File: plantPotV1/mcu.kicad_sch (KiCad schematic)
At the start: 1 part, among them U3 NUCLEO-L4R5ZI-P

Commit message: changed to meet proposal
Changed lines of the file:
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@@
 		(comment 4 "Stanford University")
+	)
+	(hierarchical_label "CS"
+		(shape output)
+		(at 134.62 52.07 0)
+		(fields_autoplaced yes)
+		(effects
+			(font
+				(size 1.27 1.27)
+			)
+			(justify left)
+		)
 	)
 	(hierarchical_label "SDA"
 		(shape output)
 		(at 110.49 50.8 0)
+		(fields_autoplaced yes)
+		(effects
+			(font
+				(size 1.27 1.27)
+			)
+			(justify left)
+		)
+	)
+	(hierarchical_label "MISO"
+		(shape input)
+		(at 134.62 48.26 0)
 		(fields_autoplaced yes)
 		(effects
@@
 		)
 	)
-	(hierarchical_label "Vmic"
-		(shape input)
-		(at 161.29 50.8 0)
-		(fields_autoplaced yes)
-		(effects
-			(font
-				(size 1.27 1.27)
-			)
-			(justify left)
-		)
-	)
-	(hierarchical_label "Vspeaker+"
+	(hierarchical_label "MTR_CTRL"
 		(shape output)
-		(at 133.35 46.99 0)
-		(fields_autoplaced yes)
-		(effects
-			(font
-				(size 1.27 1.27)
-			)
-			(justify left)
-		)
-	)
-	(hierarchical_label "Vspeaker-"
-		(shape output)
-		(at 133.35 50.8 0)
+		(at 181.61 48.26 0)
 		(fields_autoplaced yes)
 		(effects
@@
 		(fields_autoplaced yes)
 		(effects
+			(font
+				(size 1.27 1.27)
+			)
+			(justify left)
+		)
+	)
+	(hierarchical_label "MOSI"
+		(shape output)
+		(at 134.62 44.45 0)
+		(fields_autoplaced yes)
+		(effects
+			(font
+				(size 1.27 1.27)
+			)
+			(justify left)
+		)
+	)
+	(hierarchical_label "SCK"
+		(shape output)
+		(at 134.62 40.64 0)
+		(fields_autoplaced yes)
+		(effects

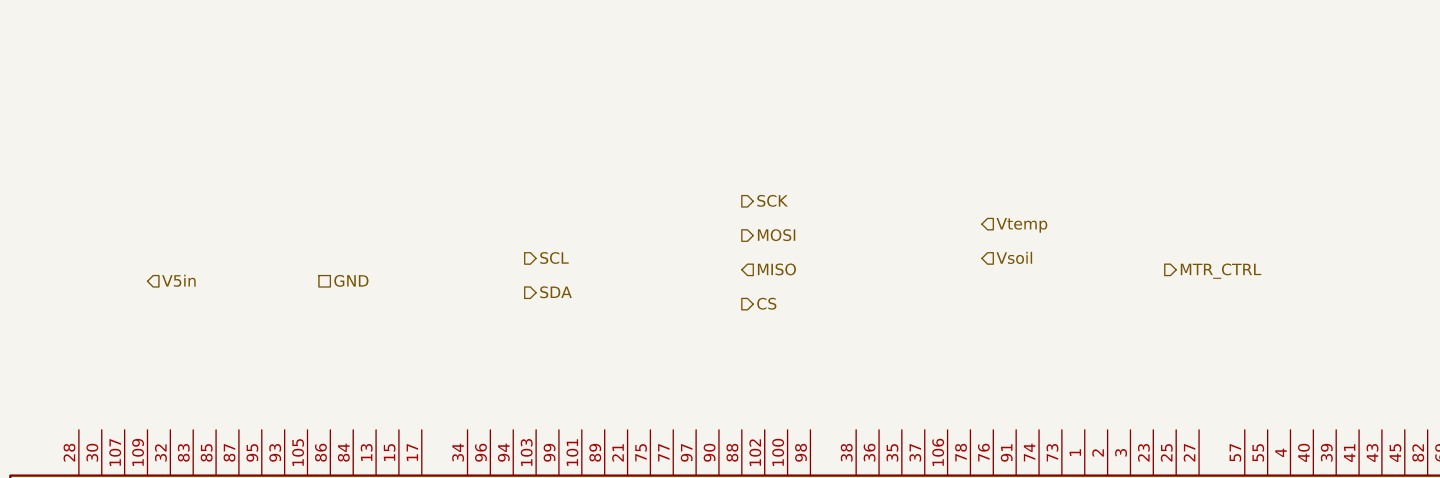
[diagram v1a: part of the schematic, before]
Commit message: updated circuit diagram (top only)
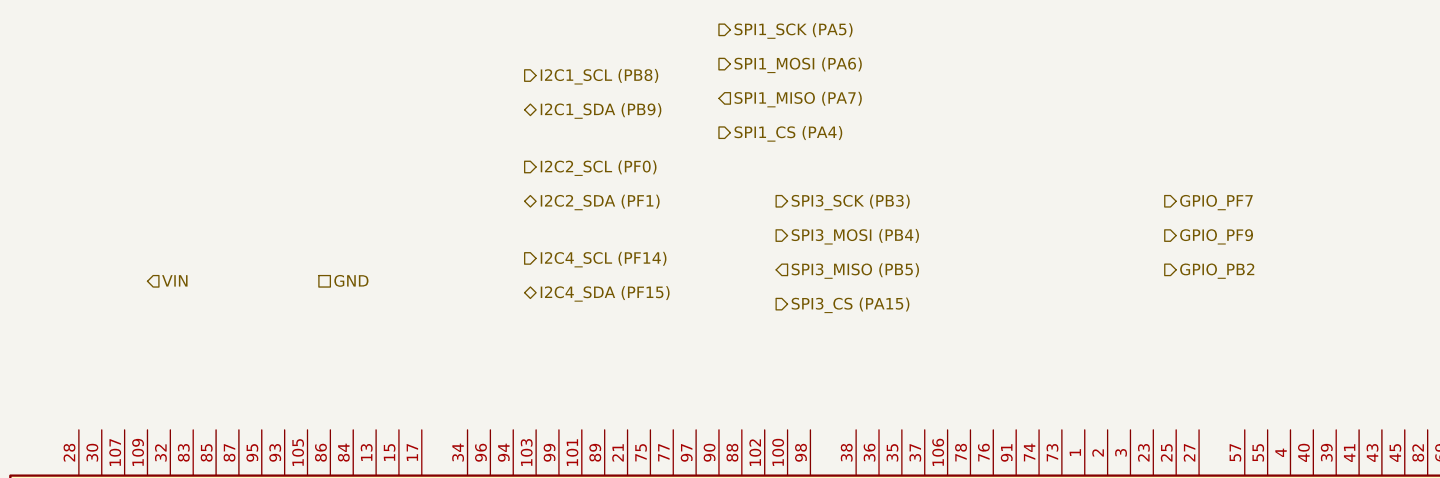
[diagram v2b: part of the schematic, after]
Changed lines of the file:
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@@
 		(comment 4 "Stanford University")
 	)
-	(hierarchical_label "CS"
-		(shape output)
-		(at 134.62 52.07 0)
-		(fields_autoplaced yes)
-		(effects
-			(font
-				(size 1.27 1.27)
-			)
-			(justify left)
-		)
-	)
-	(hierarchical_label "SDA"
-		(shape output)
+	(hierarchical_label "SPI1_CS (PA4)"
+		(shape output)
+		(at 132.08 33.02 0)
+		(fields_autoplaced yes)
+		(effects
+			(font
+				(size 1.27 1.27)
+			)
+			(justify left)
+		)
+	)
+	(hierarchical_label "I2C1_SDA (PB9)"
+		(shape bidirectional)
+		(at 110.49 30.48 0)
+		(fields_autoplaced yes)
+		(effects
+			(font
+				(size 1.27 1.27)
+			)
+			(justify left)
+		)
+	)
+	(hierarchical_label "GPIO_PF7"
+		(shape output)
+		(at 181.61 40.64 0)
+		(fields_autoplaced yes)
+		(effects
+			(font
+				(size 1.27 1.27)
+			)
+			(justify left)
+		)
+	)
+	(hierarchical_label "I2C4_SDA (PF15)"
+		(shape bidirectional)
 		(at 110.49 50.8 0)
 		(fields_autoplaced yes)
@@
 		)
 	)
-	(hierarchical_label "MISO"
+	(hierarchical_label "SPI1_MISO (PA7)"
 		(shape input)
-		(at 134.62 48.26 0)
+		(at 132.08 29.21 0)
 		(fields_autoplaced yes)
 		(effects
@@
 		)
 	)
-	(hierarchical_label "V5in"
+	(hierarchical_label "I2C2_SDA (PF1)"
+		(shape bidirectional)
+		(at 110.49 40.64 0)
+		(fields_autoplaced yes)
+		(effects
+			(font
+				(size 1.27 1.27)
+			)
+			(justify left)
+		)
+	)
+	(hierarchical_label "VIN"
 		(shape input)
 		(at 68.58 49.53 0)
@@
 		)
 	)
-	(hierarchical_label "MTR_CTRL"
+	(hierarchical_label "I2C2_SCL (PF0)"
+		(shape output)
+		(at 110.49 36.83 0)
+		(fields_autoplaced yes)
+		(effects
+			(font
+				(size 1.27 1.27)
+			)
+			(justify left)
+		)
+	)
+	(hierarchical_label "SPI3_SCK (PB3)"
+		(shape output)
+		(at 138.43 40.64 0)
+		(fields_autoplaced yes)
+		(effects
+			(font
+				(size 1.27 1.27)
+			)
+			(justify left)
+		)
+	)
+	(hierarchical_label "I2C1_SCL (PB8)"
+		(shape output)
+		(at 110.49 26.67 0)
+		(fields_autoplaced yes)
+		(effects
+			(font
+				(size 1.27 1.27)
+			)
+			(justify left)
+		)
+	)
+	(hierarchical_label "GPIO_PB2"
 		(shape output)
 		(at 181.61 48.26 0)
@@
 		)
 	)
-	(hierarchical_label "SCL"
+	(hierarchical_label "I2C4_SCL (PF14)"
 		(shape output)
 		(at 110.49 46.99 0)
@@
 		)
 	)
-	(hierarchical_label "Vtemp"
+	(hierarchical_label "GPIO_PF9"
+		(shape output)
+		(at 181.61 44.45 0)
+		(fields_autoplaced yes)
+		(effects
+			(font
+				(size 1.27 1.27)
+			)
+			(justify left)
+		)
+	)
+	(hierarchical_label "SPI1_MOSI (PA6)"
+		(shape output)
+		(at 132.08 25.4 0)
+		(fields_autoplaced yes)
+		(effects
+			(font
+				(size 1.27 1.27)
+			)
+			(justify left)
+		)
+	)
+	(hierarchical_label "SPI3_MOSI (PB4)"
+		(shape output)
+		(at 138.43 44.45 0)
+		(fields_autoplaced yes)
+		(effects
+			(font
+				(size 1.27 1.27)
+			)
+			(justify left)
+		)
+	)
+	(hierarchical_label "SPI1_SCK (PA5)"
+		(shape output)
+		(at 132.08 21.59 0)
+		(fields_autoplaced yes)
+		(effects
+			(font
+				(size 1.27 1.27)
+			)
+			(justify left)
+		)
+	)
+	(hierarchical_label "SPI3_MISO (PB5)"
 		(shape input)
-		(at 161.29 43.18 0)
-		(fields_autoplaced yes)
-		(effects
-			(font
-				(size 1.27 1.27)
-			)
-			(justify left)
-		)
-	)
-	(hierarchical_label "MOSI"
-		(shape output)
-		(at 134.62 44.45 0)
-		(fields_autoplaced yes)
-		(effects
-			(font
-				(size 1.27 1.27)
-			)
-			(justify left)
-		)
-	)
-	(hierarchical_label "SCK"
-		(shape output)
-		(at 134.62 40.64 0)
-		(fields_autoplaced yes)
-		(effects
-			(font
-				(size 1.27 1.27)
-			)
-			(justify left)
-		)
-	)
-	(hierarchical_label "Vsoil"
-		(shape input)
-		(at 161.29 46.99 0)
-		(fields_autoplaced yes)
-		(effects
+		(at 138.43 48.26 0)
+		(fields_autoplaced yes)
+		(effects
+			(font
+				(size 1.27 1.27)
+			)
+			(justify left)
+		)
+	)
+	(hierarchical_label "SPI3_CS (PA15)"
+		(shape output)
+		(at 138.43 52.07 0)
+		(fields_autoplaced yes)
+		(effects
